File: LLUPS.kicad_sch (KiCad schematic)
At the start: 37 parts, among them J1 USB_C, J2 Output, J3 Debug, Q1 FS8205A, U1 USBLC6-2SC6, U2 BQ24072, U3 HY2113-KB5B, U4 MT3608, U5 AP2112K-3.3, U6 LN61CN3302MR-G

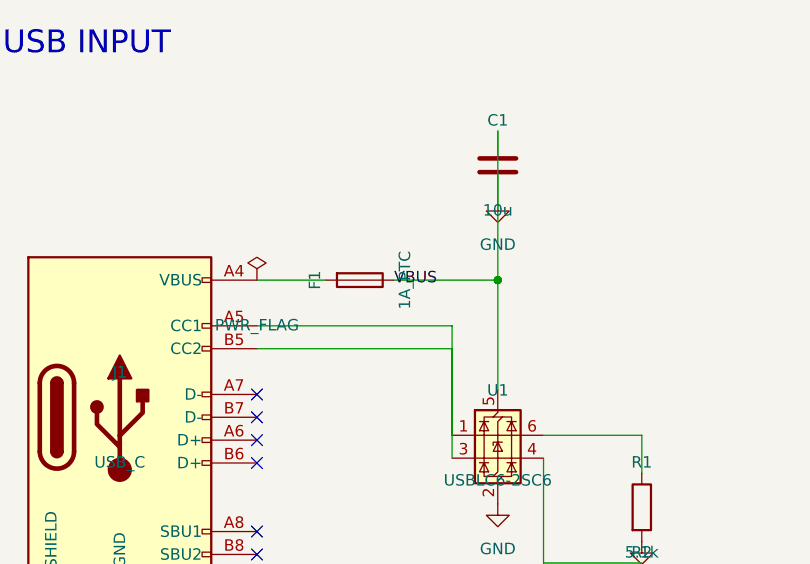
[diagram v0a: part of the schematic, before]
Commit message: Add PCB scoring framework and fix power trace widths
- scoring/ module with 6 checks: trace widths, DRC, connectivity,
  placement, vias, routing efficiency
- score_layout.py orchestrator with JSON output and --compare
- Fix power trace widths: 0.5mm → 1.0mm, 0.8mm → 1.2mm (spec: ≥1mm)
- Add 18 thermal vias under U2 (BQ24072) and U4 (MT3608)
- Score improved from 56.2 → 84.9/100

Co-Authored-By: Claude Opus 4.6 <noreply@anthropic.com>
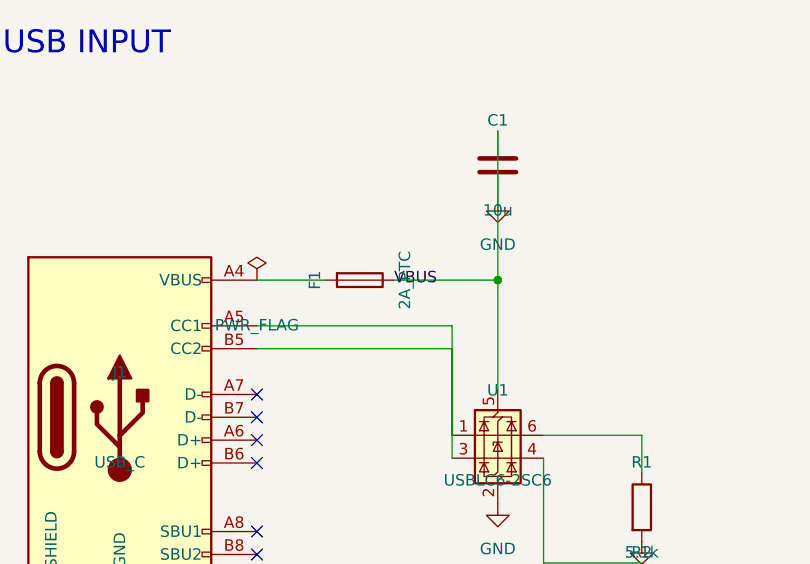
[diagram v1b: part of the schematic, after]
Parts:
- F1: value 1A_PTC -> 2A_PTC; LCSC C70061 -> (none)
